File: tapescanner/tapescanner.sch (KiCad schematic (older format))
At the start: 37 parts, among them J0 Barrel_Jack, J1 DB9_Female, J2 AVR-ISP-10, Q0 TEPT5600, Q1 TEPT5600, Q2 TEPT5600, Q3 TEPT5600, Q4 TEPT5600, Q5 TEPT5600, Q6 TEPT5600, Q7 TEPT5600, Q8 TEPT5600, Q9 TEPT5600, U0 ATmega328P-PU

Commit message: Add FT232RL
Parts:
- removed J0: Barrel_Jack, symbol Connector:Barrel_Jack
- removed J1: DB9_Female, symbol Connector:DB9_Female
- added J0: USB_B, symbol Connector:USB_B
- added U1: FT232RL, Package_SO:SSOP-28_5.3x10.2mm_P0.65mm, symbol Interface_USB:FT232RL
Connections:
- net labels removed: SERIAL_RX, SERIAL_TX
- wire segments 118 -> 128
- no-connect marks 14 -> 24
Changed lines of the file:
@@
 	0    -1   -1   0
 $EndComp
-$Comp
-L Connector:DB9_Female J1
-U 1 1 607D3CB4
-P 9750 5850
-F 0 "J1" V 9622 6405 50  0000 L CNN
-F 1 "DB9_Female" V 9713 6405 50  0000 L CNN
-F 2 "" H 9750 5850 50  0001 C CNN
-F 3 " ~" H 9750 5850 50  0001 C CNN
-	1    9750 5850
-	0    1    1    0
-$EndComp
-Text Label 9750 5550 1    50   ~ 0
-SERIAL_RX
-Text Label 9950 5550 1    50   ~ 0
-SERIAL_TX
-$Comp
-L power:GND #PWR0112
-U 1 1 607E8C7F
-P 9350 5550
-F 0 "#PWR0112" H 9350 5300 50  0001 C CNN
-F 1 "GND" H 9355 5377 50  0000 C CNN
-F 2 "" H 9350 5550 50  0001 C CNN
-F 3 "" H 9350 5550 50  0001 C CNN
-	1    9350 5550
-	-1   0    0    1
-$EndComp
-Text Label 9100 1850 2    50   ~ 0
-SERIAL_TX
-Text Label 9100 1950 2    50   ~ 0
-SERIAL_RX
 NoConn ~ 9100 1550
 NoConn ~ 9100 1650
@@
 NoConn ~ 9100 3450
 NoConn ~ 9100 3550
-NoConn ~ 9450 5550
-NoConn ~ 9550 5550
-NoConn ~ 9650 5550
-NoConn ~ 9850 5550
-NoConn ~ 10050 5550
-NoConn ~ 10150 5550
 NoConn ~ 7900 2850
 $Comp
@@
 F 3 " ~" H 6725 2800 50  0001 C CNN
 	1    8000 3350
-	1    0    0    -1
-$EndComp
-$Comp
-L power:+5V #PWR0105
-U 1 1 6065B2EA
-P 8300 5650
-F 0 "#PWR0105" H 8300 5500 50  0001 C CNN
-F 1 "+5V" V 8315 5778 50  0000 L CNN
-F 2 "" H 8300 5650 50  0001 C CNN
-F 3 "" H 8300 5650 50  0001 C CNN
-	1    8300 5650
-	0    1    1    0
-$EndComp
-$Comp
-L power:GND #PWR0106
-U 1 1 6065B711
-P 8300 5850
-F 0 "#PWR0106" H 8300 5600 50  0001 C CNN
-F 1 "GND" V 8305 5722 50  0000 R CNN
-F 2 "" H 8300 5850 50  0001 C CNN
-F 3 "" H 8300 5850 50  0001 C CNN
-	1    8300 5850
-	0    -1   -1   0
-$EndComp
-$Comp
-L power:PWR_FLAG #FLG0101
-U 1 1 6065C0B5
-P 8200 5650
-F 0 "#FLG0101" H 8200 5725 50  0001 C CNN
-F 1 "PWR_FLAG" H 8200 5823 50  0000 C CNN
-F 2 "" H 8200 5650 50  0001 C CNN
-F 3 "~" H 8200 5650 50  0001 C CNN
-	1    8200 5650
-	1    0    0    -1
-$EndComp
-Connection ~ 8200 5650
-Wire Wire Line
-	8200 5650 8300 5650
-$Comp
-L power:PWR_FLAG #FLG0102
-U 1 1 6065DAFE
-P 8200 5850
-F 0 "#FLG0102" H 8200 5925 50  0001 C CNN
-F 1 "PWR_FLAG" H 8200 6023 50  0000 C CNN
-F 2 "" H 8200 5850 50  0001 C CNN
-F 3 "~" H 8200 5850 50  0001 C CNN
-	1    8200 5850
-	-1   0    0    1
-$EndComp
-Connection ~ 8200 5850
-Wire Wire Line
-	8200 5850 8300 5850
-Wire Wire Line
-	7950 5650 8200 5650
-Wire Wire Line
-	7950 5850 8200 5850
-$Comp
-L Connector:Barrel_Jack J0
-U 1 1 606418E7
-P 7650 5750
-F 0 "J0" H 7707 6075 50  0000 C CNN
-F 1 "Barrel_Jack" H 7707 5984 50  0000 C CNN
-F 2 "" H 7700 5710 50  0001 C CNN
-F 3 "~" H 7700 5710 50  0001 C CNN
-	1    7650 5750
 	1    0    0    -1
 $EndComp
@@
 $EndComp
 $Comp
-L power:GND #PWR?
+L power:GND #PWR0105
 U 1 1 6053249A
 P 10100 4150
-F 0 "#PWR?" H 10100 3900 50  0001 C CNN
+F 0 "#PWR0105" H 10100 3900 50  0001 C CNN
 F 1 "GND" V 10105 4022 50  0000 R CNN
 F 2 "" H 10100 4150 50  0001 C CNN
@@
 	0    -1   -1   0
 $EndComp
+$Comp
+L Interface_USB:FT232RL U1
+U 1 1 605C6AF0
+P 6400 2550
+F 0 "U1" H 6400 3731 50  0000 C CNN
+F 1 "FT232RL" H 6400 3640 50  0000 C CNN
+F 2 "Package_SO:SSOP-28_5.3x10.2mm_P0.65mm" H 7500 1650 50  0001 C CNN
+F 3 "https://www.ftdichip.com/Support/Documents/DataSheets/ICs/DS_FT232R.pdf" H 6400 2550 50  0001 C CNN
+	1    6400 2550
+	1    0    0    -1
+$EndComp
+$Comp
+L Connector:USB_B J0
+U 1 1 605CF6FE
+P 5000 2150
+F 0 "J0" H 5057 2617 50  0000 C CNN
+F 1 "USB_B" H 5057 2526 50  0000 C CNN
+F 2 "" H 5150 2100 50  0001 C CNN
+F 3 " ~" H 5150 2100 50  0001 C CNN
+	1    5000 2150
+	1    0    0    -1
+$EndComp
+NoConn ~ 5600 2550
+NoConn ~ 5600 2750
+NoConn ~ 5600 2950
+$Comp
+L power:GND #PWR0106
+U 1 1 605F6BDE
+P 5600 3250
+F 0 "#PWR0106" H 5600 3000 50  0001 C CNN
+F 1 "GND" V 5605 3122 50  0000 R CNN
+F 2 "" H 5600 3250 50  0001 C CNN
+F 3 "" H 5600 3250 50  0001 C CNN
+	1    5600 3250
+	0    1    1    0
+$EndComp
+NoConn ~ 4900 2550
+NoConn ~ 7200 2850
+NoConn ~ 7200 2950
+NoConn ~ 7200 3050
+NoConn ~ 7200 3150
+NoConn ~ 7200 3250
+NoConn ~ 7200 2550
+NoConn ~ 7200 2450
+NoConn ~ 7200 2350
+NoConn ~ 7200 2250
+NoConn ~ 7200 2150
+NoConn ~ 7200 2050
+$Comp
+L power:GND #PWR0112
+U 1 1 6062A9F6
+P 5000 2550
+F 0 "#PWR0112" H 5000 2300 50  0001 C CNN
+F 1 "GND" H 5005 2377 50  0000 C CNN
+F 2 "" H 5000 2550 50  0001 C CNN
+F 3 "" H 5000 2550 50  0001 C CNN
+	1    5000 2550
+	1    0    0    -1
+$EndComp
+$Comp
+L power:+5V #PWR0114
+U 1 1 6063DFAE
+P 5300 1950
+F 0 "#PWR0114" H 5300 1800 50  0001 C CNN
+F 1 "+5V" V 5315 2078 50  0000 L CNN
+F 2 "" H 5300 1950 50  0001 C CNN
+F 3 "" H 5300 1950 50  0001 C CNN
+	1    5300 1950
+	0    1    1    0
+$EndComp
+$Comp
+L power:+5V #PWR0115
+U 1 1 6064034E
+P 6300 1550
+F 0 "#PWR0115" H 6300 1400 50  0001 C CNN
+F 1 "+5V" H 6315 1723 50  0000 C CNN
+F 2 "" H 6300 1550 50  0001 C CNN
+F 3 "" H 6300 1550 50  0001 C CNN
+	1    6300 1550
+	1    0    0    -1
+$EndComp
+$Comp
+L power:+5V #PWR0116
+U 1 1 606407DD
+P 6500 1550
+F 0 "#PWR0116" H 6500 1400 50  0001 C CNN
+F 1 "+5V" H 6515 1723 50  0000 C CNN
+F 2 "" H 6500 1550 50  0001 C CNN
+F 3 "" H 6500 1550 50  0001 C CNN
+	1    6500 1550
+	1    0    0    -1
+$EndComp
+Wire Wire Line
+	6200 3550 6200 3650
+Wire Wire Line
+	6200 3650 6400 3650
+Wire Wire Line
+	6400 3650 6400 3550
+Wire Wire Line
+	6400 3650 6500 3650
+Wire Wire Line
+	6500 3650 6500 3550
+Connection ~ 6400 3650
+Wire Wire Line
+	6600 3550 6600 3650
+Wire Wire Line
+	6600 3650 6500 3650
+Connection ~ 6500 3650
+Wire Wire Line
+	6200 3650 6050 3650
+Connection ~ 6200 3650
+$Comp
+L power:GND #PWR0117
+U 1 1 60659DF5
+P 6050 3650
+F 0 "#PWR0117" H 6050 3400 50  0001 C CNN
+F 1 "GND" V 6055 3522 50  0000 R CNN
+F 2 "" H 6050 3650 50  0001 C CNN
+F 3 "" H 6050 3650 50  0001 C CNN
+	1    6050 3650
+	0    1    1    0
+$EndComp
+Wire Wire Line
+	9100 1850 9000 1950
+Wire Wire Line
+	7200 1950 9000 1950
+Wire Wire Line
+	7200 1850 9000 1850
+Wire Wire Line
+	9000 1850 9100 1950
+NoConn ~ 5600 1850
+Wire Wire Line
+	5300 2150 5600 2150
+Wire Wire Line
+	5600 2250 5300 2250
 $EndSCHEMATC

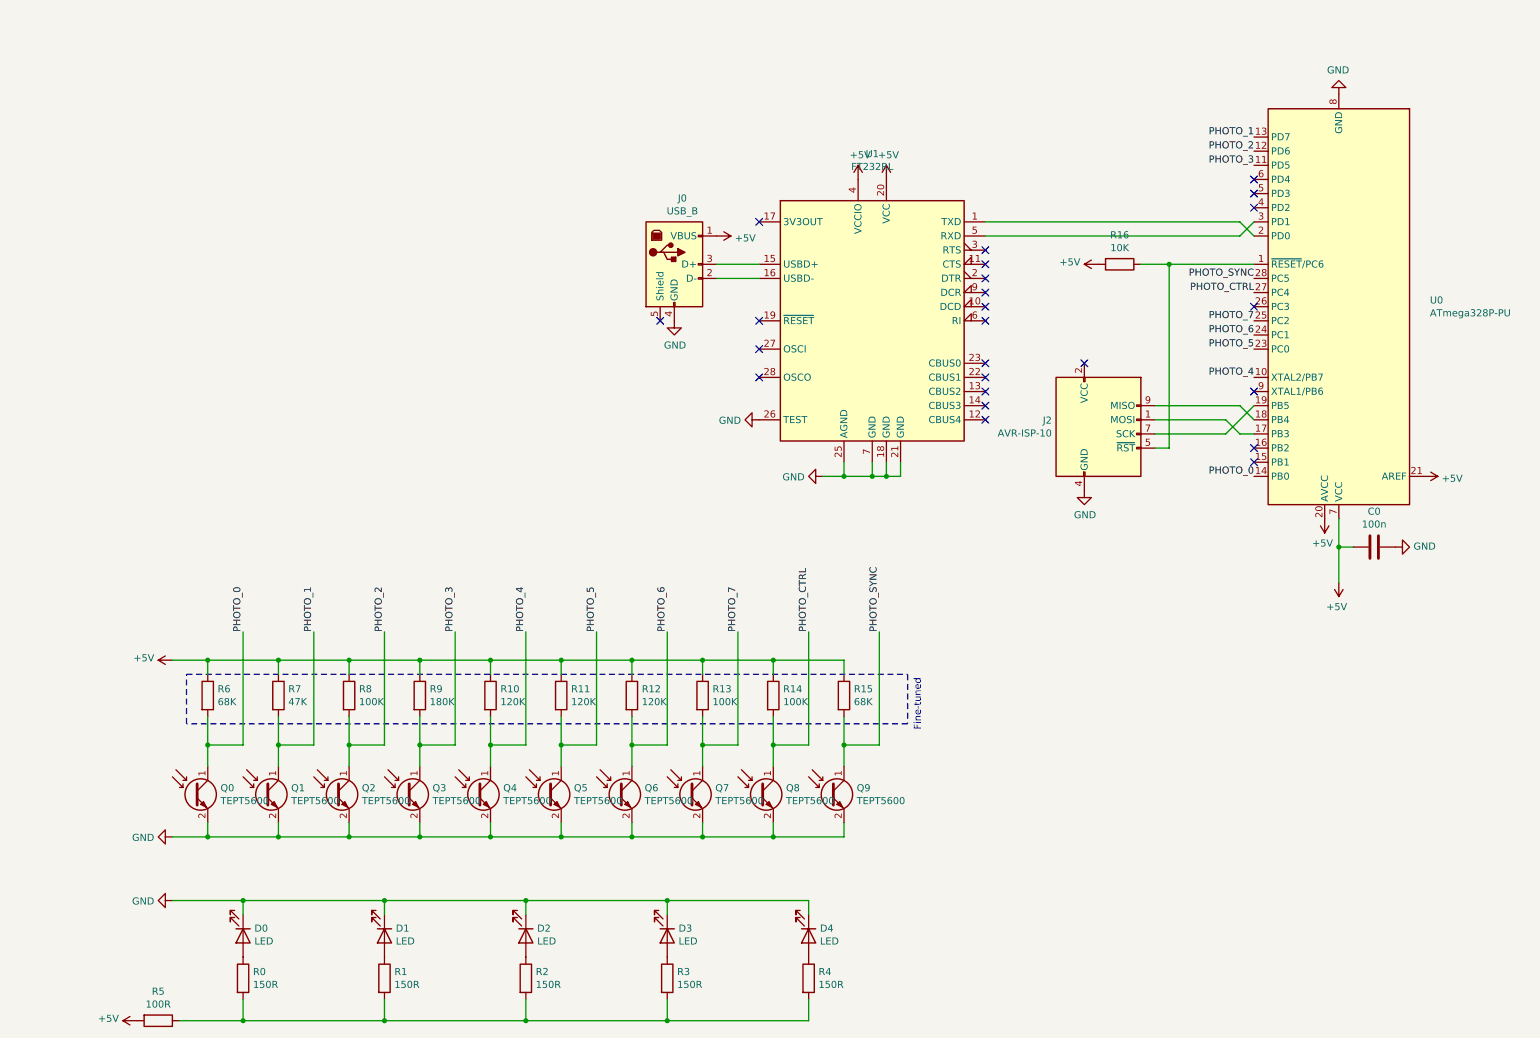
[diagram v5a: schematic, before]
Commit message: Add motor and power switching circuit
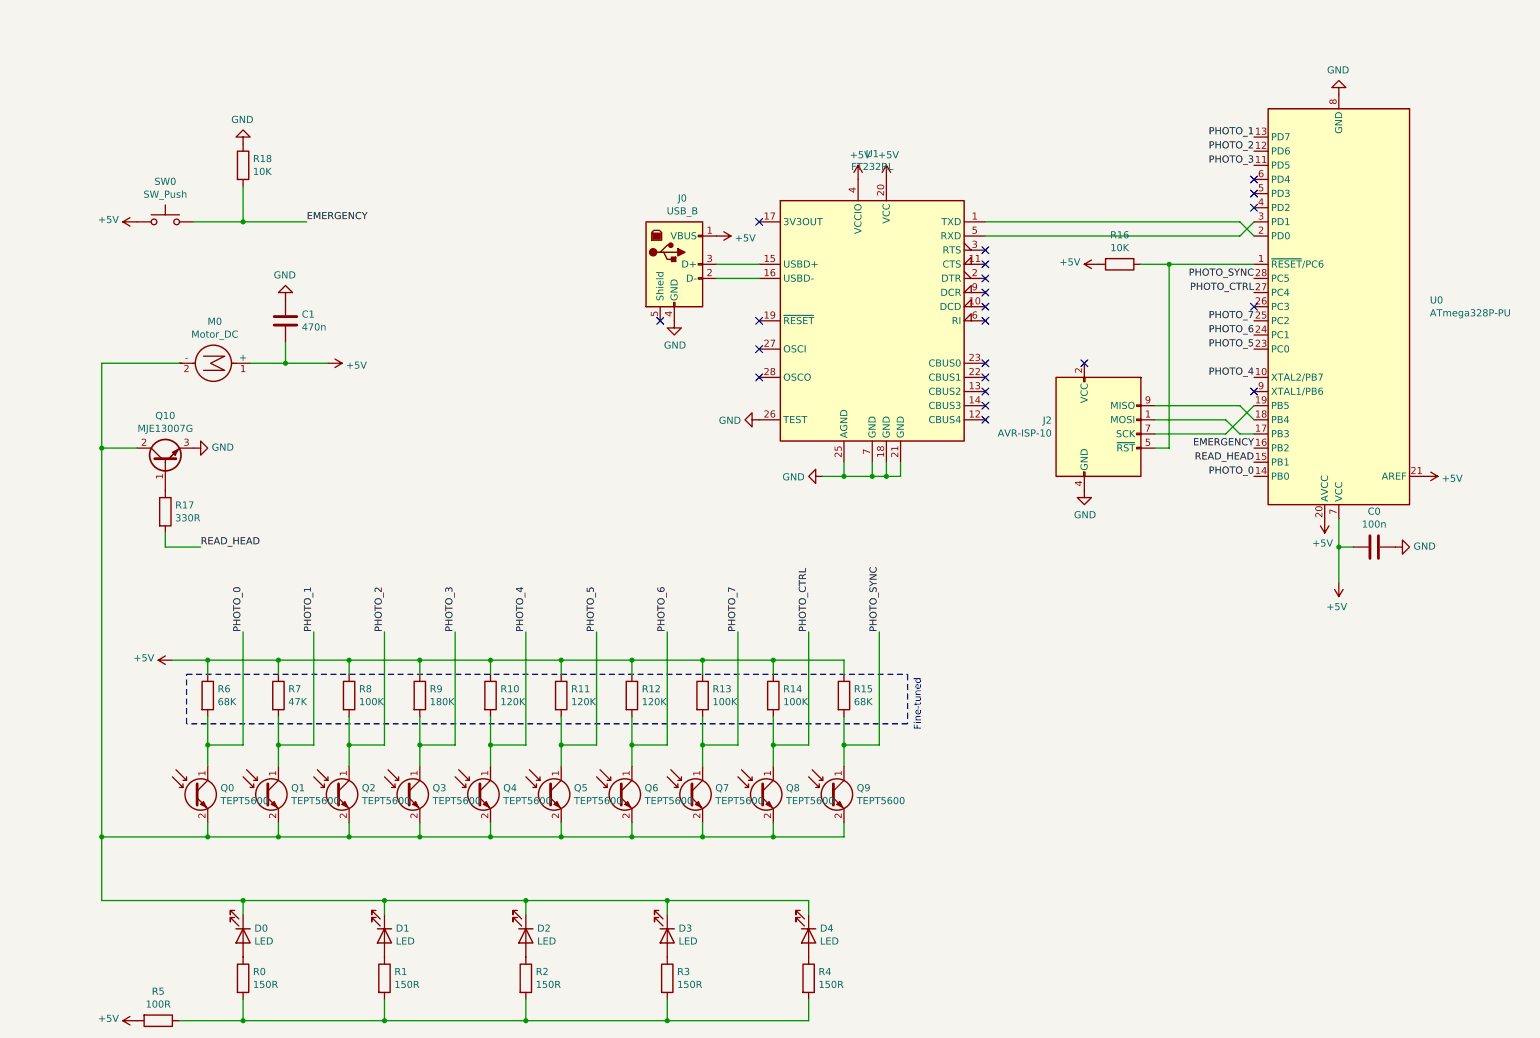
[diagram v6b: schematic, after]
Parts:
- added C1: 470n, symbol Device:C
- added M0: Motor_DC, symbol Motor:Motor_DC
- added Q10: MJE13007G, Package_TO_SOT_THT:TO-220-3_Vertical, symbol Transistor_BJT:MJE13007G
- added R17: 330R, symbol Device:R
- added R18: 10K, symbol Device:R
- added SW0: SW_Push, symbol Switch:SW_Push
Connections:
- net +5V: now also C1.2, M0.1 (+), SW0.1
- net GND: now also C1.1, Q10.3 (E), R18.1; no longer D0.1 (K), D1.1 (K), D2.1 (K), D3.1 (K), D4.1 (K), Q0.2 (E), Q1.2 (E), Q2.2 (E), Q3.2 (E), Q4.2 (E), Q5.2 (E), Q6.2 (E), Q7.2 (E), Q8.2 (E), Q9.2 (E)
- net READ_HEAD: now reaches U0.15 (PB1)
- net READ_HEAD: now also R17.2
- net EMERGENCY: now reaches U0.16 (PB2)
- net EMERGENCY: now also R18.2, SW0.2
- new net: D0.1 (K), D1.1 (K), D2.1 (K), D3.1 (K), D4.1 (K), M0.2 (-), Q0.2 (E), Q1.2 (E), Q10.2 (C), Q2.2 (E), Q3.2 (E), Q4.2 (E), Q5.2 (E), Q6.2 (E), Q7.2 (E), Q8.2 (E), Q9.2 (E)
- new net: Q10.1 (B), R17.1
- no-connect marks 24 -> 22
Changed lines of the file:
@@
 Wire Wire Line
 	1700 4950 2200 4950
-$Comp
-L power:GND #PWR0104
-U 1 1 605F46FB
-P 1450 6200
-F 0 "#PWR0104" H 1450 5950 50  0001 C CNN
-F 1 "GND" V 1455 6072 50  0000 R CNN
-F 2 "" H 1450 6200 50  0001 C CNN
-F 3 "" H 1450 6200 50  0001 C CNN
-	1    1450 6200
-	0    1    1    0
-$EndComp
 Connection ~ 5700 6200
 Wire Wire Line
@@
 Wire Wire Line
 	2200 6200 2700 6200
-Connection ~ 1700 6200
 Wire Wire Line
 	1700 6200 2200 6200
@@
 Wire Wire Line
 	3700 5550 3950 5550
-$Comp
-L power:GND #PWR0101
-U 1 1 604C259B
-P 1450 6650
-F 0 "#PWR0101" H 1450 6400 50  0001 C CNN
-F 1 "GND" V 1455 6522 50  0000 R CNN
-F 2 "" H 1450 6650 50  0001 C CNN
-F 3 "" H 1450 6650 50  0001 C CNN
-	1    1450 6650
-	0    1    1    0
-$EndComp
 Wire Wire Line
 	1450 4950 1700 4950
-Wire Wire Line
-	1450 6200 1700 6200
-$Comp
-L Sensor_Optical:TEPT4400 Q0
-U 1 1 604B7B85
-P 1600 5900
-F 0 "Q0" H 1790 5946 50  0000 L CNN
-F 1 "TEPT5600" H 1790 5855 50  0000 L CNN
-F 2 "LED_THT:LED_D3.0mm_Clear" H 2080 5760 50  0001 C CNN
-F 3 "https://www.vishay.com/docs/84768/tept5600.pdf" H 1600 5900 50  0001 C CNN
-	1    1600 5900
-	1    0    0    -1
-$EndComp
 Wire Wire Line
 	4950 6650 5950 6650
@@
 Wire Wire Line
 	1950 6650 2950 6650
-Connection ~ 1950 6650
 Wire Wire Line
 	1950 7500 2950 7500
@@
 Wire Wire Line
 	1500 7500 1950 7500
-Wire Wire Line
-	1450 6650 1950 6650
 Wire Wire Line
 	6450 4750 6450 5550
@@
 NoConn ~ 9100 2450
 NoConn ~ 9100 3050
-NoConn ~ 9100 3450
-NoConn ~ 9100 3550
 NoConn ~ 7900 2850
 $Comp
@@
 	1    7900 3750
 	1    0    0    -1
-$EndComp
-$Comp
-L MCU_Microchip_ATmega:ATmega328P-PU U0
-U 1 1 607AED4A
-P 9700 2450
-F 0 "U0" H 9056 2404 50  0000 R CNN
-F 1 "ATmega328P-PU" H 9056 2495 50  0000 R CNN
-F 2 "Package_DIP:DIP-28_W7.62mm" H 9700 2450 50  0001 C CIN
-F 3 "http://ww1.microchip.com/downloads/en/DeviceDoc/ATmega328_P%20AVR%20MCU%20with%20picoPower%20Technology%20Data%20Sheet%2040001984A.pdf" H 9700 2450 50  0001 C CNN
-	1    9700 2450
-	-1   0    0    1
 $EndComp
 Wire Wire Line
@@
 Wire Wire Line
 	5600 2250 5300 2250
+$Comp
+L MCU_Microchip_ATmega:ATmega328P-PU U0
+U 1 1 607AED4A
+P 9700 2450
+F 0 "U0" H 9056 2404 50  0000 R CNN
+F 1 "ATmega328P-PU" H 9056 2495 50  0000 R CNN
+F 2 "Package_DIP:DIP-28_W7.62mm" H 9700 2450 50  0001 C CIN
+F 3 "http://ww1.microchip.com/downloads/en/DeviceDoc/ATmega328_P%20AVR%20MCU%20with%20picoPower%20Technology%20Data%20Sheet%2040001984A.pdf" H 9700 2450 50  0001 C CNN
+	1    9700 2450
+	-1   0    0    1
+$EndComp
+Text Label 9100 3550 2    50   ~ 0
+READ_HEAD
+Text Label 9100 3450 2    50   ~ 0
+EMERGENCY
+$Comp
+L Transistor_BJT:MJE13007G Q10
+U 1 1 606AAE77
+P 1400 3550
+F 0 "Q10" V 1729 3550 50  0000 C CNN
+F 1 "MJE13007G" V 1638 3550 50  0000 C CNN
+F 2 "Package_TO_SOT_THT:TO-220-3_Vertical" H 1650 3475 50  0001 L CIN
+F 3 "http://www.onsemi.com/pub_link/Collateral/MJE13007-D.PDF" H 1400 3550 50  0001 L CNN
+	1    1400 3550
+	0    -1   -1   0
+$EndComp
+$Comp
+L power:GND #PWR?
+U 1 1 606B3702
+P 1600 3450
+F 0 "#PWR?" H 1600 3200 50  0001 C CNN
+F 1 "GND" V 1605 3322 50  0000 R CNN
+F 2 "" H 1600 3450 50  0001 C CNN
+F 3 "" H 1600 3450 50  0001 C CNN
+	1    1600 3450
+	0    -1   -1   0
+$EndComp
+Connection ~ 1950 6650
+$Comp
+L Sensor_Optical:TEPT4400 Q0
+U 1 1 604B7B85
+P 1600 5900
+F 0 "Q0" H 1790 5946 50  0000 L CNN
+F 1 "TEPT5600" H 1790 5855 50  0000 L CNN
+F 2 "LED_THT:LED_D3.0mm_Clear" H 2080 5760 50  0001 C CNN
+F 3 "https://www.vishay.com/docs/84768/tept5600.pdf" H 1600 5900 50  0001 C CNN
+	1    1600 5900
+	1    0    0    -1
+$EndComp
+Connection ~ 1700 6200
+Wire Wire Line
+	1200 3450 950  3450
+Wire Wire Line
+	950  6650 1950 6650
+Wire Wire Line
+	950  6200 1700 6200
+Wire Wire Line
+	950  6200 950  6650
+$Comp
+L Device:R R17
+U 1 1 606CF734
+P 1400 3900
+F 0 "R17" H 1470 3946 50  0000 L CNN
+F 1 "330R" H 1470 3855 50  0000 L CNN
+F 2 "" V 1330 3900 50  0001 C CNN
+F 3 "~" H 1400 3900 50  0001 C CNN
+	1    1400 3900
+	1    0    0    -1
+$EndComp
+Wire Wire Line
+	1400 4050 1400 4150
+Wire Wire Line
+	1400 4150 1650 4150
+Text Label 1650 4150 0    50   ~ 0
+READ_HEAD
+Wire Wire Line
+	950  2850 1500 2850
+$Comp
+L Motor:Motor_DC M0
+U 1 1 606DC4B7
+P 1800 2850
+F 0 "M0" V 1505 2800 50  0000 C CNN
+F 1 "Motor_DC" V 1596 2800 50  0000 C CNN
+F 2 "" H 1800 2760 50  0001 C CNN
+F 3 "~" H 1800 2760 50  0001 C CNN
+	1    1800 2850
+	0    1    1    0
+$EndComp
+Wire Wire Line
+	2000 2850 2250 2850
+Wire Wire Line
+	2250 2850 2250 2700
+Connection ~ 2250 2850
+Wire Wire Line
+	2250 2850 2550 2850
+$Comp
+L Device:C C1
+U 1 1 606EDAE3
+P 2250 2550
+F 0 "C1" H 2365 2596 50  0000 L CNN
+F 1 "470n" H 2365 2505 50  0000 L CNN
+F 2 "" H 2288 2400 50  0001 C CNN
+F 3 "~" H 2250 2550 50  0001 C CNN
+	1    2250 2550
+	1    0    0    -1
+$EndComp
+$Comp
+L power:GND #PWR?
+U 1 1 606EFFCB
+P 2250 2400
+F 0 "#PWR?" H 2250 2150 50  0001 C CNN
+F 1 "GND" H 2255 2227 50  0000 C CNN
+F 2 "" H 2250 2400 50  0001 C CNN
+F 3 "" H 2250 2400 50  0001 C CNN
+	1    2250 2400
+	-1   0    0    1
+$EndComp
+$Comp
+L power:+5V #PWR?
+U 1 1 606F04F9
+P 2550 2850
+F 0 "#PWR?" H 2550 2700 50  0001 C CNN
+F 1 "+5V" V 2565 2978 50  0000 L CNN
+F 2 "" H 2550 2850 50  0001 C CNN
+F 3 "" H 2550 2850 50  0001 C CNN
+	1    2550 2850
+	0    1    1    0
+$EndComp
+Wire Wire Line
+	950  3450 950  6200
+Connection ~ 950  6200
+Wire Wire Line
+	950  2850 950  3450
+Connection ~ 950  3450
+$Comp
+L Switch:SW_Push SW0
+U 1 1 60725EDE
+P 1400 1850
+F 0 "SW0" H 1400 2135 50  0000 C CNN
+F 1 "SW_Push" H 1400 2044 50  0000 C CNN
+F 2 "" H 1400 2050 50  0001 C CNN
+F 3 "~" H 1400 2050 50  0001 C CNN
+	1    1400 1850
+	1    0    0    -1
+$EndComp
+$Comp
+L power:+5V #PWR?
+U 1 1 60727D38
+P 1200 1850
+F 0 "#PWR?" H 1200 1700 50  0001 C CNN
+F 1 "+5V" V 1215 1978 50  0000 L CNN
+F 2 "" H 1200 1850 50  0001 C CNN
+F 3 "" H 1200 1850 50  0001 C CNN
+	1    1200 1850
+	0    -1   -1   0
+$EndComp
+Text Label 2400 1850 0    50   ~ 0
+EMERGENCY
+$Comp
+L Device:R R18
+U 1 1 60739369
+P 1950 1450
+F 0 "R18" H 2020 1496 50  0000 L CNN
+F 1 "10K" H 2020 1405 50  0000 L CNN
+F 2 "" V 1880 1450 50  0001 C CNN
+F 3 "~" H 1950 1450 50  0001 C CNN
+	1    1950 1450
+	1    0    0    -1
+$EndComp
+$Comp
+L power:GND #PWR?
+U 1 1 6073B5AB
+P 1950 1300
+F 0 "#PWR?" H 1950 1050 50  0001 C CNN
+F 1 "GND" H 1955 1127 50  0000 C CNN
+F 2 "" H 1950 1300 50  0001 C CNN
+F 3 "" H 1950 1300 50  0001 C CNN
+	1    1950 1300
+	-1   0    0    1
+$EndComp
+Wire Wire Line
+	1600 1850 1950 1850
+Wire Wire Line
+	1950 1600 1950 1850
+Connection ~ 1950 1850
+Wire Wire Line
+	1950 1850 2400 1850
 $EndSCHEMATC
